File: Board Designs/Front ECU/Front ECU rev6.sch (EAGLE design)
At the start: 87 parts, among them IC2 OKI-78SR, IC3 OKI-78SR, X1 CONNECTOR-4, X2 CONNECTOR-4, X3 CONNECTOR-4MX150L_VERTICAL-4, X4 CONNECTOR-10MX150L_VERTICAL-10, X5 CONNECTOR-10MX150L_VERTICAL-10, X6 CONNECTOR-10MX150L_VERTICAL-10

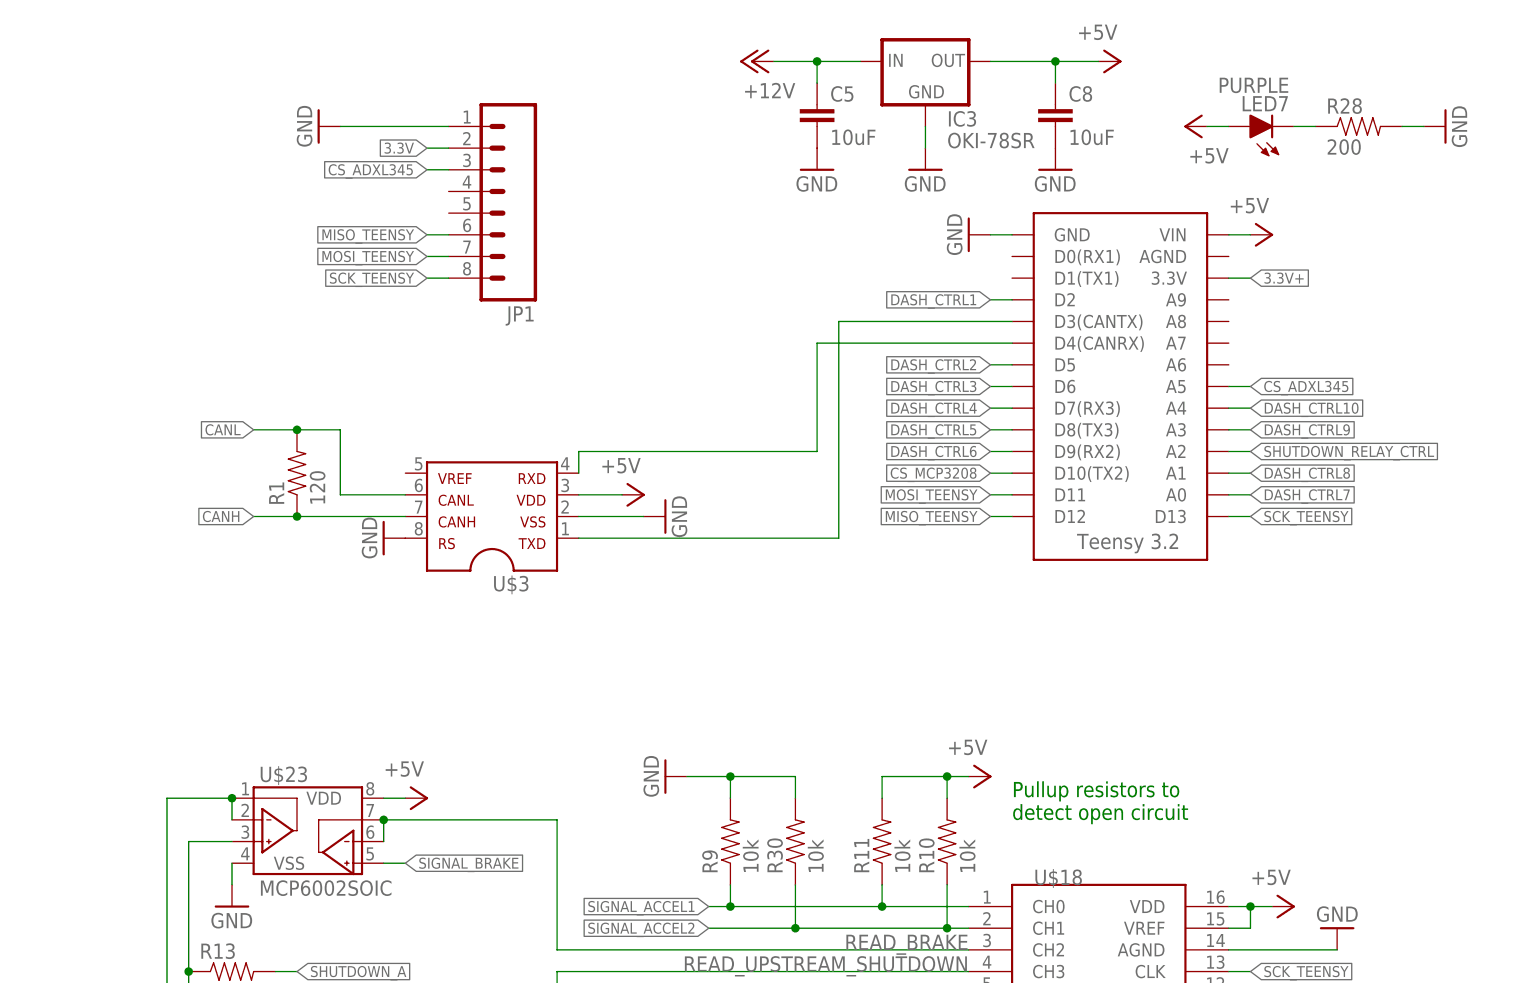
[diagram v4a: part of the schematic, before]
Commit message: BMS rev7: use NPN regulator instead of buck converter, Front ECU rev6: Use I2C for accelerometer, HV Board rev4: Add shutdown circuit line to BMS ADC, External diagrams for both competitions
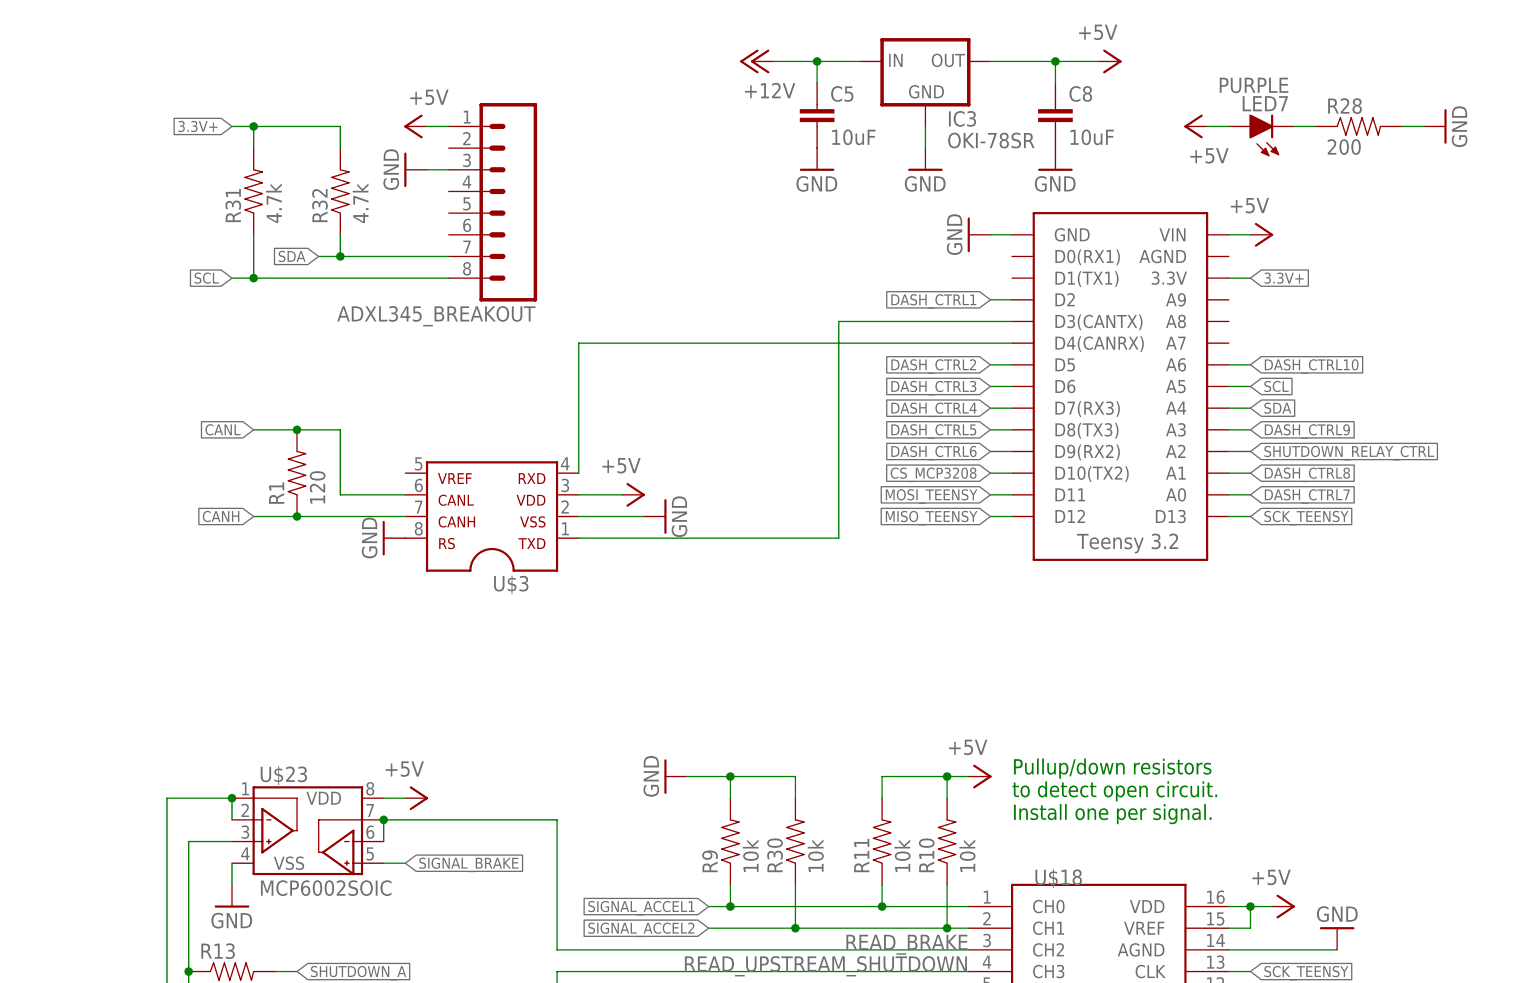
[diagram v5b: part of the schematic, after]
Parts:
- added R31, R32: 4.7k, HyTechDevices:RESISTOR0805-RES
- renumbered JP1 to ADXL345_BREAKOUT
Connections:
- removed net 3.3V: ADXL345_BREAKOUT.2
- removed net CS_ADXL345: ADXL345_BREAKOUT.3, U$1.A5
- new net SCL: ADXL345_BREAKOUT.8, R31.1, U$1.A5
- new net SDA: ADXL345_BREAKOUT.7, R32.1, U$1.A4
- net +5V: now also ADXL345_BREAKOUT.1
- net 3.3V+: now also R31.2, R32.2
- net DASH_CTRL10: now also U$1.A6; no longer U$1.A4
- net GND: now also ADXL345_BREAKOUT.3; no longer ADXL345_BREAKOUT.1
- net MISO_TEENSY: no longer ADXL345_BREAKOUT.6
- net MOSI_TEENSY: no longer ADXL345_BREAKOUT.7
- net SCK_TEENSY: no longer ADXL345_BREAKOUT.8
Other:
- note added: "Microcontroller, Accelerometer, and Power"
- note added: "Pullup/down resistors to detect open circuit. Install one per signal."
- note removed: "Microcontroller and Power"
- note removed: "Pullup resistors to detect open circuit"
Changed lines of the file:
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@@
 <?xml version="1.0" encoding="utf-8"?>
 <!DOCTYPE eagle SYSTEM "eagle.dtd">
-<eagle version="8.6.3">
+<eagle version="8.4.1">
 <drawing>
 <settings>
@@
 <part name="GND35" library="HyTechSymbols" deviceset="GND" device=""/>
 <part name="GND36" library="HyTechSymbols" deviceset="GND" device=""/>
-<part name="JP1" library="HyTechDevices" deviceset="M08" device=""/>
+<part name="ADXL345_BREAKOUT" library="HyTechDevices" deviceset="M08" device=""/>
+<part name="P+20" library="supply1" library_urn="urn:adsk.eagle:library:371" deviceset="+5V" device=""/>
+<part name="R31" library="HyTechDevices" deviceset="RESISTOR" device="0805-RES" value="4.7k"/>
+<part name="R32" library="HyTechDevices" deviceset="RESISTOR" device="0805-RES" value="4.7k"/>
 </parts>
 <sheets>
@@
 <wire x1="269.24" y1="167.64" x2="269.24" y2="238.76" width="0.1524" layer="90"/>
 <wire x1="269.24" y1="238.76" x2="111.76" y2="238.76" width="0.1524" layer="90"/>
-<text x="111.76" y="238.76" size="5.08" layer="90">Microcontroller and Power</text>
+<text x="111.76" y="238.76" size="5.08" layer="90">Microcontroller, Accelerometer, and Power</text>
 <wire x1="0" y1="238.76" x2="0" y2="0" width="0.1524" layer="90"/>
 <wire x1="0" y1="0" x2="104.14" y2="0" width="0.1524" layer="90"/>
@@
 <text x="314.96" y="17.78" size="1.778" layer="91">Use these jumpers to select
 DASH_IO{7,8} output voltage</text>
-<text x="213.36" y="144.78" size="1.778" layer="91">Pullup resistors to
-detect open circuit</text>
+<text x="213.36" y="144.78" size="1.778" layer="91">Pullup/down resistors
+to detect open circuit.
+Install one per signal.</text>
 </plain>
 <moduleinsts>
@@
 <instance part="R30" gate="G$1" x="187.96" y="142.24" rot="R90"/>
 <instance part="GND35" gate="1" x="172.72" y="149.86" rot="R270"/>
-<instance part="GND36" gate="1" x="132.08" y="226.06" rot="R270"/>
-<instance part="JP1" gate="G$1" x="152.4" y="218.44" rot="R180"/>
+<instance part="GND36" gate="1" x="142.24" y="220.98" rot="R270"/>
+<instance part="ADXL345_BREAKOUT" gate="G$1" x="152.4" y="218.44" rot="R180"/>
+<instance part="P+20" gate="1" x="142.24" y="226.06" rot="MR270"/>
+<instance part="R31" gate="G$1" x="124.46" y="218.44" rot="R90"/>
+<instance part="R32" gate="G$1" x="134.62" y="218.44" rot="R90"/>
 </instances>
 <busses>
@@
 </segment>
 <segment>
+<pinref part="ADXL345_BREAKOUT" gate="G$1" pin="3"/>
 <pinref part="GND36" gate="1" pin="GND"/>
-<wire x1="147.32" y1="226.06" x2="134.62" y2="226.06" width="0.1524" layer="91"/>
-<pinref part="JP1" gate="G$1" pin="1"/>
+<wire x1="144.78" y1="220.98" x2="147.32" y2="220.98" width="0.1524" layer="91"/>
 </segment>
 </net>
@@
 <junction x="205.74" y="149.86"/>
 </segment>
+<segment>
+<pinref part="ADXL345_BREAKOUT" gate="G$1" pin="1"/>
+<pinref part="P+20" gate="1" pin="+5V"/>
+<wire x1="144.78" y1="226.06" x2="147.32" y2="226.06" width="0.1524" layer="91"/>
+</segment>
 </net>
 <net name="N$2" class="0">
 <segment>
 <pinref part="U$3" gate="G$1" pin="4"/>
-<wire x1="162.56" y1="185.42" x2="162.56" y2="187.96" width="0.1524" layer="91"/>
+<wire x1="162.56" y1="185.42" x2="162.56" y2="200.66" width="0.1524" layer="91"/>
 <pinref part="U$1" gate="G$1" pin="D4(CANRX)"/>
-<wire x1="162.56" y1="187.96" x2="190.5" y2="187.96" width="0.1524" layer="91"/>
-<wire x1="190.5" y1="187.96" x2="190.5" y2="200.66" width="0.1524" layer="91"/>
-<wire x1="190.5" y1="200.66" x2="213.36" y2="200.66" width="0.1524" layer="91"/>
+<wire x1="162.56" y1="200.66" x2="213.36" y2="200.66" width="0.1524" layer="91"/>
 </segment>
 </net>
@@
 </segment>
 <segment>
-<label x="241.3" y="193.04" size="1.27" layer="95" xref="yes"/>
-<pinref part="U$1" gate="G$1" pin="A4"/>
-<wire x1="241.3" y1="193.04" x2="238.76" y2="193.04" width="0.1524" layer="91"/>
+<label x="241.3" y="198.12" size="1.27" layer="95" xref="yes"/>
+<pinref part="U$1" gate="G$1" pin="A6"/>
+<wire x1="238.76" y1="198.12" x2="241.3" y2="198.12" width="0.1524" layer="91"/>
 </segment>
 </net>
@@
 <label x="241.3" y="127" size="1.27" layer="95" xref="yes"/>
 </segment>
-<segment>
-<wire x1="147.32" y1="208.28" x2="144.78" y2="208.28" width="0.1524" layer="91"/>
-<label x="144.78" y="208.28" size="1.27" layer="95" rot="R180" xref="yes"/>
-<pinref part="JP1" gate="G$1" pin="8"/>
-</segment>
 </net>
 <net name="MISO_TEENSY" class="0">
@@
 <wire x1="210.82" y1="180.34" x2="213.36" y2="180.34" width="0.1524" layer="91"/>
 </segment>
-<segment>
-<wire x1="147.32" y1="213.36" x2="144.78" y2="213.36" width="0.1524" layer="91"/>
-<label x="144.78" y="213.36" size="1.27" layer="95" rot="R180" xref="yes"/>
-<pinref part="JP1" gate="G$1" pin="6"/>
-</segment>
 </net>
 <net name="MOSI_TEENSY" class="0">
@@
 <pinref part="U$1" gate="G$1" pin="D11"/>
 <wire x1="210.82" y1="182.88" x2="213.36" y2="182.88" width="0.1524" layer="91"/>
-</segment>
-<segment>
-<wire x1="147.32" y1="210.82" x2="144.78" y2="210.82" width="0.1524" layer="91"/>
-<label x="144.78" y="210.82" size="1.27" layer="95" rot="R180" xref="yes"/>
-<pinref part="JP1" gate="G$1" pin="7"/>
 </segment>
 </net>
@@
 <label x="241.3" y="208.28" size="1.27" layer="95" xref="yes"/>
 </segment>
-</net>
-<net name="3.3V" class="0">
-<segment>
-<wire x1="147.32" y1="223.52" x2="144.78" y2="223.52" width="0.1524" layer="91"/>
-<label x="144.78" y="223.52" size="1.27" layer="95" rot="R180" xref="yes"/>
-<pinref part="JP1" gate="G$1" pin="2"/>
-</segment>
-</net>
-<net name="CS_ADXL345" class="0">
-<segment>
-<wire x1="147.32" y1="220.98" x2="144.78" y2="220.98" width="0.1524" layer="91"/>
-<label x="144.78" y="220.98" size="1.27" layer="95" rot="R180" xref="yes"/>
-<pinref part="JP1" gate="G$1" pin="3"/>
-</segment>
+<segment>
+<pinref part="R31" gate="G$1" pin="2"/>
+<wire x1="124.46" y1="223.52" x2="124.46" y2="226.06" width="0.1524" layer="91"/>
+<wire x1="124.46" y1="226.06" x2="134.62" y2="226.06" width="0.1524" layer="91"/>
+<pinref part="R32" gate="G$1" pin="2"/>
+<wire x1="134.62" y1="226.06" x2="134.62" y2="223.52" width="0.1524" layer="91"/>
+<wire x1="124.46" y1="226.06" x2="121.92" y2="226.06" width="0.1524" layer="91"/>
+<junction x="124.46" y="226.06"/>
+<label x="121.92" y="226.06" size="1.27" layer="95" rot="R180" xref="yes"/>
+</segment>
+</net>
+<net name="SCL" class="0">
 <segment>
 <pinref part="U$1" gate="G$1" pin="A5"/>
@@
 <label x="241.3" y="195.58" size="1.27" layer="95" xref="yes"/>
 </segment>
-</net>
+<segment>
+<pinref part="R31" gate="G$1" pin="1"/>
+<pinref part="ADXL345_BREAKOUT" gate="G$1" pin="8"/>
+<wire x1="147.32" y1="208.28" x2="124.46" y2="208.28" width="0.1524" layer="91"/>
+<wire x1="124.46" y1="208.28" x2="124.46" y2="213.36" width="0.1524" layer="91"/>
+<wire x1="124.46" y1="208.28" x2="121.92" y2="208.28" width="0.1524" layer="91"/>
+<junction x="124.46" y="208.28"/>
+<label x="121.92" y="208.28" size="1.27" layer="95" rot="R180" xref="yes"/>
+</segment>
+</net>
+<net name="SDA" class="0">
+<segment>
+<pinref part="U$1" gate="G$1" pin="A4"/>
+<wire x1="238.76" y1="193.04" x2="241.3" y2="193.04" width="0.1524" layer="91"/>
+<label x="241.3" y="193.04" size="1.27" layer="95" xref="yes"/>
+</segment>
+<segment>
+<pinref part="ADXL345_BREAKOUT" gate="G$1" pin="7"/>
+<wire x1="147.32" y1="210.82" x2="134.62" y2="210.82" width="0.1524" layer="91"/>
+<pinref part="R32" gate="G$1" pin="1"/>
+<wire x1="134.62" y1="210.82" x2="134.62" y2="213.36" width="0.1524" layer="91"/>
+<wire x1="134.62" y1="210.82" x2="132.08" y2="210.82" width="0.1524" layer="91"/>
+<junction x="134.62" y="210.82"/>
+<label x="132.08" y="210.82" size="1.27" layer="95" rot="R180" xref="yes"/>
+</segment>
+</net>
